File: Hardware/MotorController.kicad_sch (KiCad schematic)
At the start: 9 parts, among them U3 STSPIN250

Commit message: Fix Traces
trace fixes
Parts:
- renumbered U3 to U4
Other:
- note added: "Motor Controller Whats the VRef about? - The Vref = Rsnsx * I_load(peak) Which means that if the back EMF of the motor goes above Vref do the shutdown sequence, this means that the Vref sets the Current Control. Therefore, the reason we need to put a Filter on the Ref pin. is to convert the Digital output of the MCU to an Analog output for purposes of current control."
- note removed: "Motor Controller Whats the Fucking VRef about? - The Vref = Rsnsx * I_load(peak) Which means that if the back EMF of the motor goes above Vref do the shutdown sequence, this means that the Vref sets the Current Control. Therefore, the reason we need to put a Filter on the Ref pin. is to convert the Digital output of the MCU to an Analog output for purposes of current control."
- title: STSPIN250 Module -> TurtleBot Mainboard
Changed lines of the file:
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@@
   (paper "A4")
   (title_block
-    (title "STSPIN250 Module")
-    (date "2022-11-26")
-    (rev "0.1")
+    (title "TurtleBot Mainboard")
+    (date "2022-11-27")
+    (rev "${REVISION}")
     (company "Amoskeag Technologies")
+    (comment 4 "${FULL_REVISION}")
   )
   (junction (at 165.1 101.6) (diameter 0) (color 0 0 0 0)
@@
     (effects (font (size 3 3)) (justify left bottom))
   )
-  (text "Motor Controller\n\nWhats the Fucking VRef about?\n\n- The Vref = Rsnsx * I_load(peak)\n\nWhich means that if the back EMF of the motor goes above Vref do the shutdown sequence, this means that the Vref sets the Current Control. \n\nTherefore, the reason we need to put a Filter on the Ref pin. is to convert the Digital output of the MCU to an Analog output for purposes of current control."
+  (text "Motor Controller\n\nWhats the VRef about?\n\n- The Vref = Rsnsx * I_load(peak)\n\nWhich means that if the back EMF of the motor goes above Vref do the shutdown sequence, this means that the Vref sets the Current Control. \n\nTherefore, the reason we need to put a Filter on the Ref pin. is to convert the Digital output of the MCU to an Analog output for purposes of current control."
     (at 16.51 34.29 0)
     (effects (font (size 1.27 1.27)) (justify left bottom))
@@
   (symbol (lib_id "power:+3.3V") (at 148.59 76.2 0) (mirror y) (unit 1)
     (in_bom yes) (on_board yes)
-    (property "Reference" "#PWR017" (id 0) (at 148.59 80.01 0)
+    (property "Reference" "#PWR023" (id 0) (at 148.59 80.01 0)
       (effects (font (size 1.27 1.27)) hide)
     )
@@
   (symbol (lib_id "power:GND") (at 162.56 85.09 0) (mirror y) (unit 1)
     (in_bom yes) (on_board yes) (fields_autoplaced)
-    (property "Reference" "#PWR019" (id 0) (at 162.56 91.44 0)
+    (property "Reference" "#PWR025" (id 0) (at 162.56 91.44 0)
       (effects (font (size 1.27 1.27)) hide)
     )
@@
   (symbol (lib_id "power:GND") (at 128.27 144.78 0) (unit 1)
     (in_bom yes) (on_board yes) (fields_autoplaced)
-    (property "Reference" "#PWR016" (id 0) (at 128.27 151.13 0)
+    (property "Reference" "#PWR022" (id 0) (at 128.27 151.13 0)
       (effects (font (size 1.27 1.27)) hide)
     )
@@
   (symbol (lib_id "Amoskeag-KiCAD-Lib:STSPIN250") (at 148.59 95.25 0) (unit 1)
     (in_bom yes) (on_board yes) (fields_autoplaced)
-    (property "Reference" "U3" (id 0) (at 150.6094 92.71 0)
+    (property "Reference" "U4" (id 0) (at 150.6094 92.71 0)
       (effects (font (size 1.27 1.27)) (justify left))
     )
@@
   (symbol (lib_id "power:GND") (at 114.3 124.46 0) (unit 1)
     (in_bom yes) (on_board yes) (fields_autoplaced)
-    (property "Reference" "#PWR015" (id 0) (at 114.3 130.81 0)
+    (property "Reference" "#PWR021" (id 0) (at 114.3 130.81 0)
       (effects (font (size 1.27 1.27)) hide)
     )
@@
   (symbol (lib_id "power:GND") (at 148.59 144.78 0) (unit 1)
     (in_bom yes) (on_board yes) (fields_autoplaced)
-    (property "Reference" "#PWR018" (id 0) (at 148.59 151.13 0)
+    (property "Reference" "#PWR024" (id 0) (at 148.59 151.13 0)
       (effects (font (size 1.27 1.27)) hide)
     )
@@
   (symbol (lib_id "power:GND") (at 166.37 144.78 0) (unit 1)
     (in_bom yes) (on_board yes) (fields_autoplaced)
-    (property "Reference" "#PWR020" (id 0) (at 166.37 151.13 0)
+    (property "Reference" "#PWR026" (id 0) (at 166.37 151.13 0)
       (effects (font (size 1.27 1.27)) hide)
     )
@@
   (symbol (lib_id "power:GND") (at 173.99 85.09 0) (mirror y) (unit 1)
     (in_bom yes) (on_board yes) (fields_autoplaced)
-    (property "Reference" "#PWR021" (id 0) (at 173.99 91.44 0)
-      (effects (font (size 1.27 1.27)) hide)
-    )
+    (property "Reference" "#PWR027" (id 0) (at 173.99 91.44 0)
+      (effects (font (size 1.27 1.27)) hide)
+    )

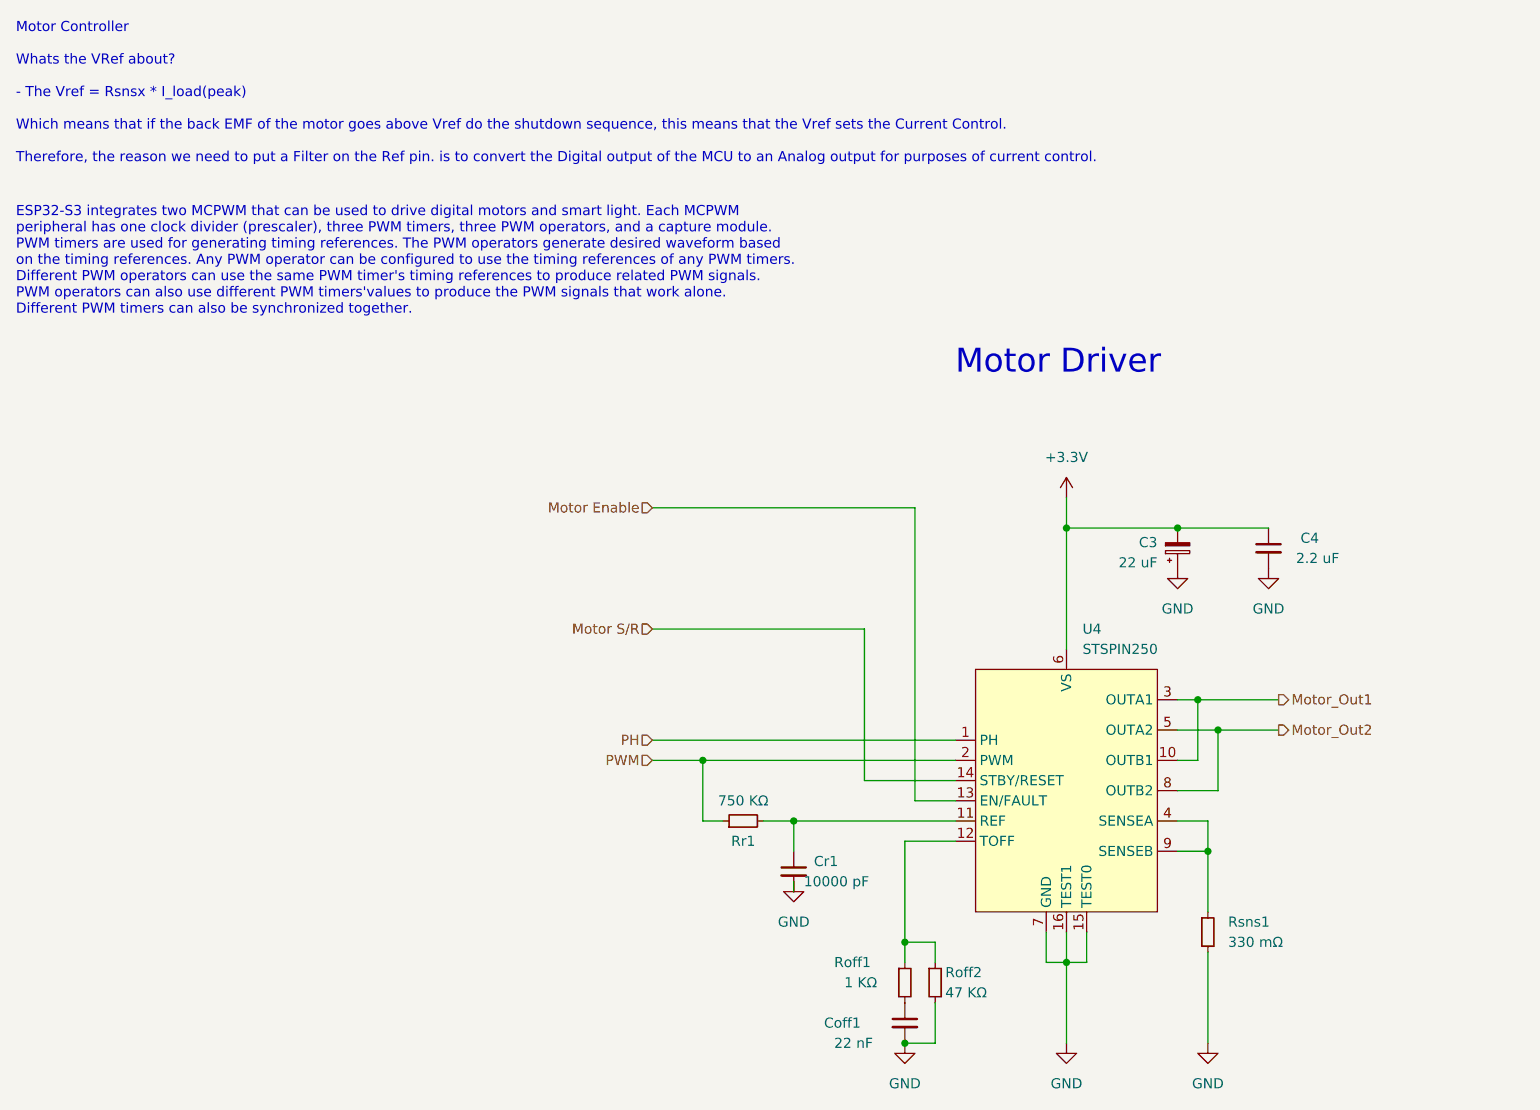
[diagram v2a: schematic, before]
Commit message: Squashed commit of the following:
commit e6d18f1838a18780ff985c290e2821e2ac438ddc
Author: KenwoodFox <kenwood364@gmail.com>
Date:   Sun Oct 5 18:23:23 2025 -0400

    Tweaked n' fixed things with @Amoskeag

commit 133f082a76a13551d058af83ac953c852f82cbfb
Author: Arthur Aznive <61330561+Amoskeag@users.noreply.github.com>
Date:   Sun Oct 5 10:51:39 2025 -0400

    Update I2C Bus Connections

    Channel 4 of I2C was not connected, will make traces pretty later.

commit 1fc084a3994e8cc2965589d6eb11268a7396225d
Author: Arthur Aznive <61330561+Amoskeag@users.noreply.github.com>
Date:   Sun Oct 5 10:36:15 2025 -0400

    Board Refactor, Updated Parts

    Updated Board layout and added new parts

commit 6f7fc722645cc0153b695158322b161c2f880b4a
Author: Arthur Aznive <61330561+Amoskeag@users.noreply.github.com>
Date:   Fri Oct 3 23:22:42 2025 -0400

    update 2025

    board refactor

commit 2a13c54343b839d82b0e646e49a68070081abc7a
Author: Arthur Aznive <61330561+Amoskeag@users.noreply.github.com>
Date:   Fri Oct 3 23:04:47 2025 -0400

    Square Board Time

    Rerouting, restarting project, trying to make a simpler dev board. Lets see what we can do.

commit d4ab96b311134bb0a7992d948496d7b671a058de
Author: Arthur Aznive <61330561+Amoskeag@users.noreply.github.com>
Date:   Wed Jan 15 14:01:24 2025 -0500

    4 L:ayer Board with USB-C

    Created a 4-Layer PCB with USB-C updates

commit 55621a658c07626f43cd5cc55c172a27abc51e41
Author: Arthur Aznive <61330561+Amoskeag@users.noreply.github.com>
Date:   Tue Mar 5 00:57:37 2024 -0500

    Updated Motor Driver Routing

    Working on Power Supply and Motor Controller Routing

commit 3f2874cc29094c27990d838de84f4fea139067e1
Author: Arthur Aznive <61330561+Amoskeag@users.noreply.github.com>
Date:   Sun Mar 3 23:13:56 2024 -0500

    BIG Changes

    Create a 4 Layer Variation
    Change Motor Controller routing.
    Change Power Regulation.
    Optimize Sensor routing.
    Pray I know what i'm doing

commit 08b48da4672d4d2e9f554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
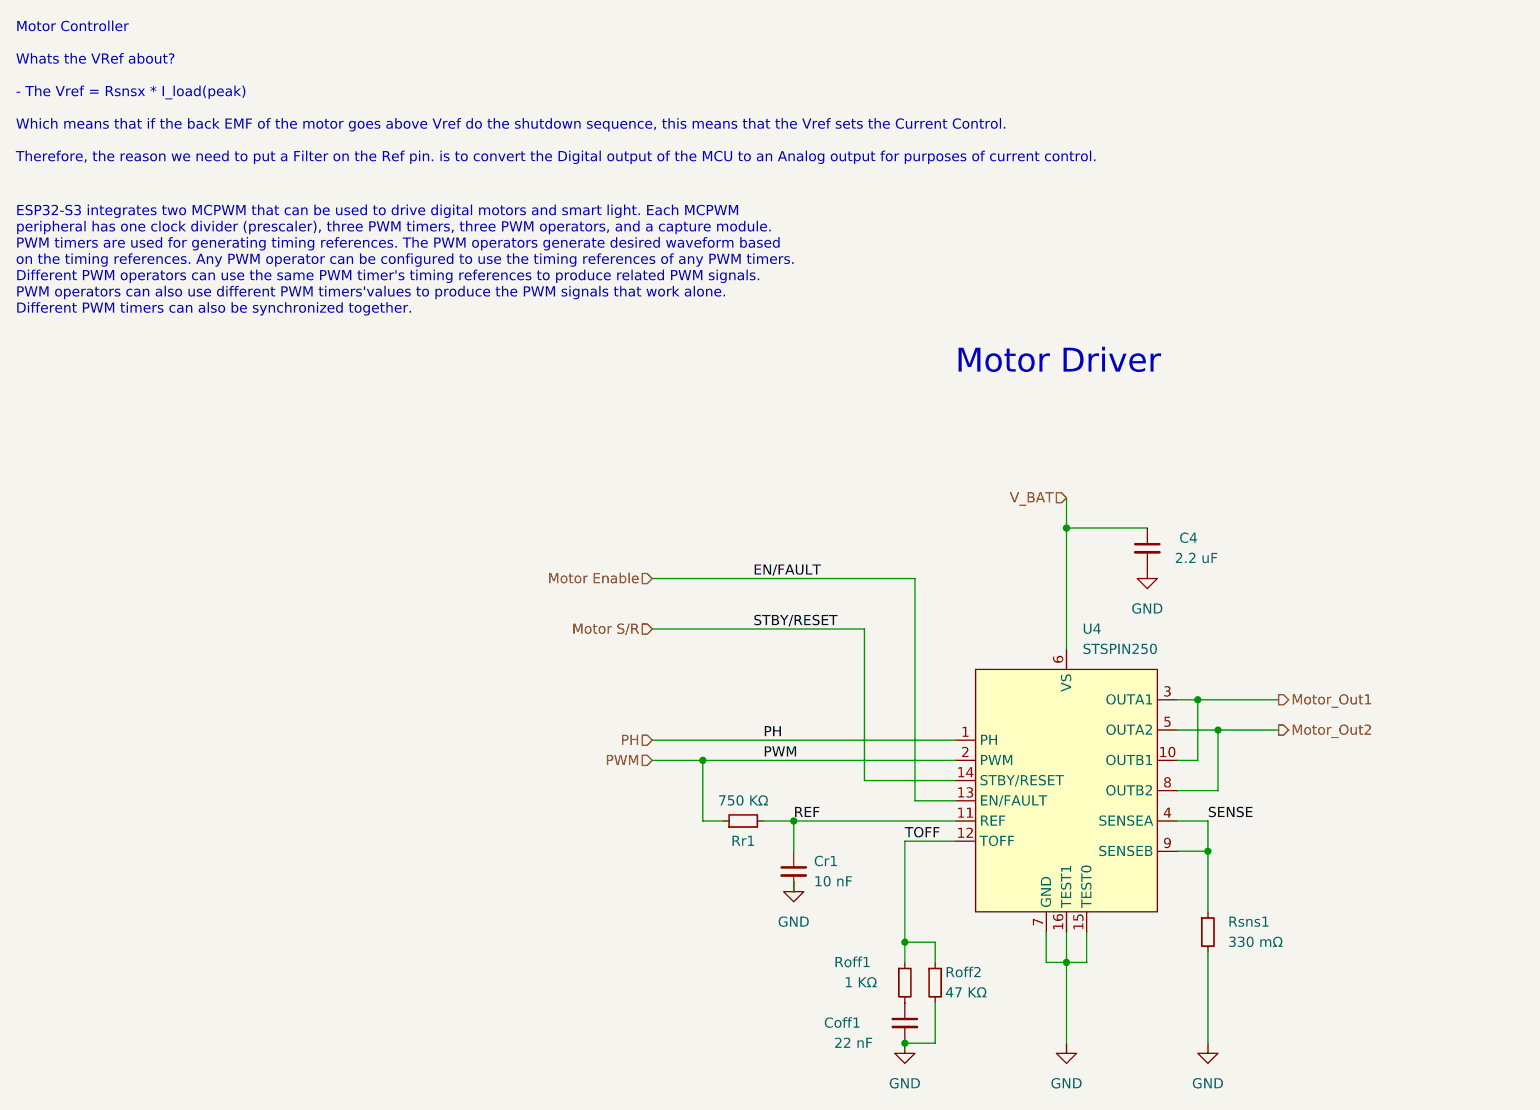
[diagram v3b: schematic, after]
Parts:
- removed C3: 22 uF, Capacitor_SMD:C_0805_2012Metric, symbol Device:C_Polarized_Small
- C4, Coff1: footprint Capacitor_SMD:C_0805_2012Metric -> Capacitor_SMD:C_0603_1608Metric
- Cr1: value 10000 pF -> 10 nF; footprint Capacitor_SMD:C_0805_2012Metric -> Capacitor_SMD:C_0603_1608Metric
- Roff1, Roff2, Rr1: footprint Resistor_SMD:R_0805_2012Metric -> Resistor_SMD:R_0603_1608Metric
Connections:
- net SENSE: now reaches Rsns1.1, U4.4 (SENSEA), U4.9 (SENSEB)
- net TOFF: now reaches Roff1.1, Roff2.1, U4.12 (TOFF)
- net REF: now reaches Cr1.1, Rr1.2, U4.11 (REF)
- net +3V3 renamed V_BAT
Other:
- moved on the sheet: C4

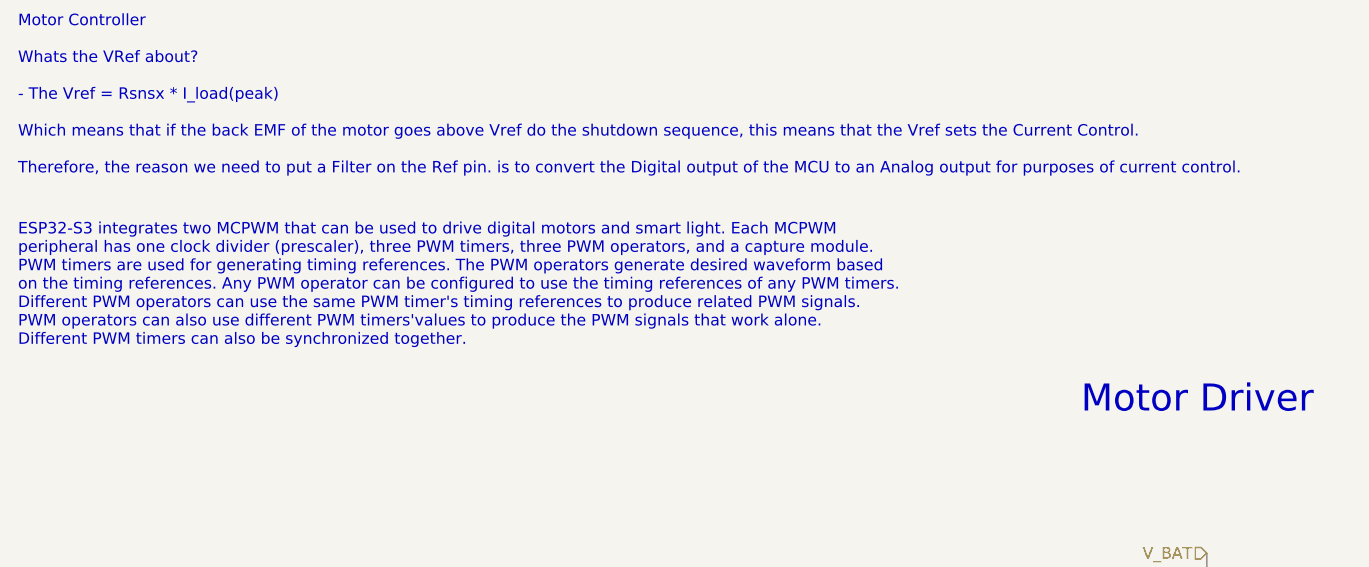
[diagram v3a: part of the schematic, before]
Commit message: Clean Up Schematic
Fixed Schematic notes, and formatting
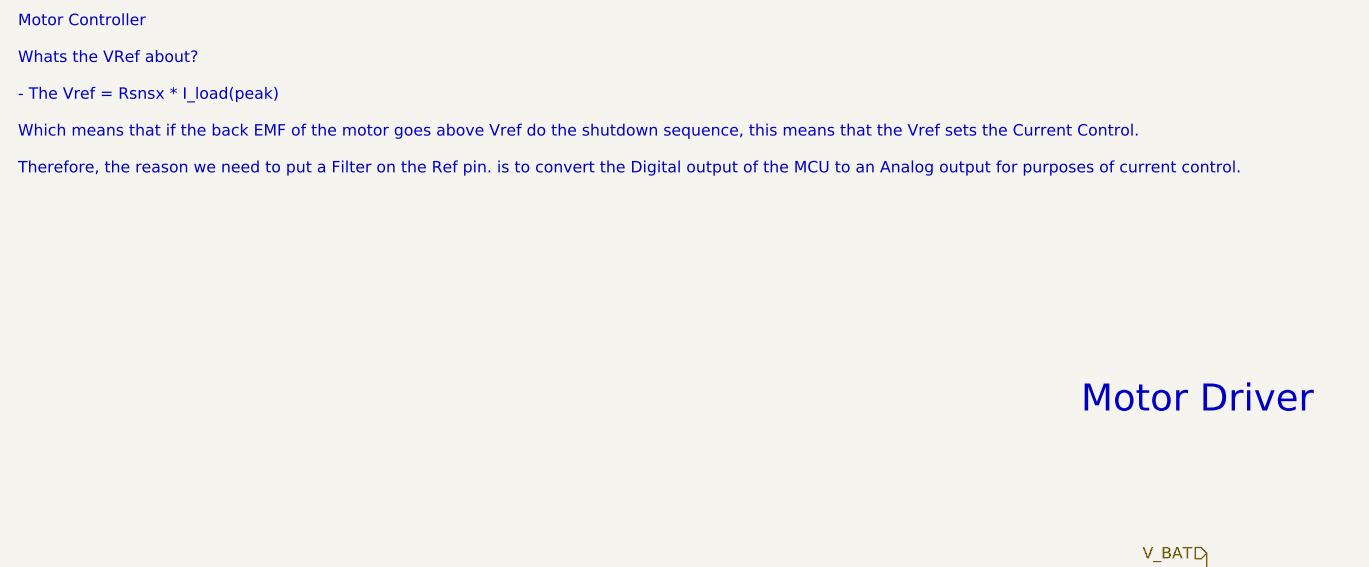
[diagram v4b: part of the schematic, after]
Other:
- note removed: "ESP32-S3 integrates two MCPWM that can be used to drive digital motors and smart light. Each MCPWM peripheral has one clock divider (prescaler), three PWM timers, three PWM operators, and a capture module. PWM timers are used for generating timing references. The PWM operators generate desired waveform based on the timing references. Any PWM operator can be configured to use the timing references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"
- title: TurtleBot Mainboard -> RoboDojo Motor Controller
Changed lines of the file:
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@@
 	(paper "A4")
 	(title_block
-		(title "TurtleBot Mainboard")
+		(title "RoboDojo Motor Controller")
 		(date "2022-11-27")
 		(rev "${REVISION}")
@@
 		(effects
 			(font
-				(size 1.27 1.27)
-			)
-			(justify left bottom)
-		)
-	)
-	(text "ESP32-S3 integrates two MCPWM that can be used to drive digital motors and smart light. Each MCPWM\nperipheral has one clock divider (prescaler), three PWM timers, three PWM operators, and a capture module.\nPWM timers are used for generating timing references. The PWM operators generate desired waveform based\non the timing references. Any PWM operator can be configured to use the timing references of any PWM timers.\nDifferent PWM operators can use the same PWM timer's timing references to produce related PWM signals.\nPWM operators can also use different PWM timers'values to produce the PWM signals that work alone.\nDifferent PWM timers can also be synchronized together.\n"
-		(exclude_from_sim no)
-		(at 16.51 53.34 0)
-		(effects
-			(font
